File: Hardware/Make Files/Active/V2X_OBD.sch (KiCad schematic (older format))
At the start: 87 parts, among them J1 DB9, P4 DB-9 to OBD2, P5 NVM_RST, Q1 2N7000, Q10 2N3904, Q2 BSS84, Q3 BSS84, Q4 BSS84, Q5 3906, Q6 2N3904, Q7 2N7000, Q8 2N3904, Q9 2N3904, SW1 SPST, U10 MCP2551, U5 ESDAxxSC6, U6 ESDAxxSC6, U7 STN1110, U8 LM339, U9 LM317, X2 16MHz

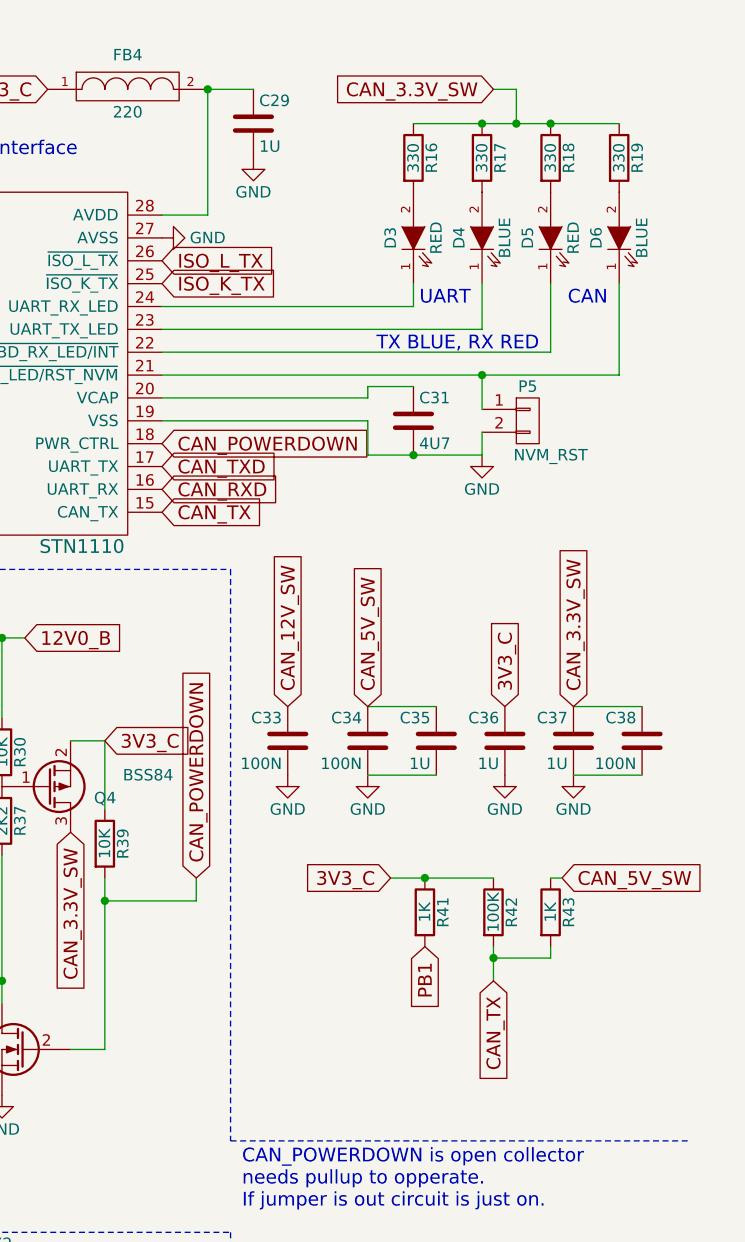
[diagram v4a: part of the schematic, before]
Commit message: Build pass of main V2X board
ready to verify
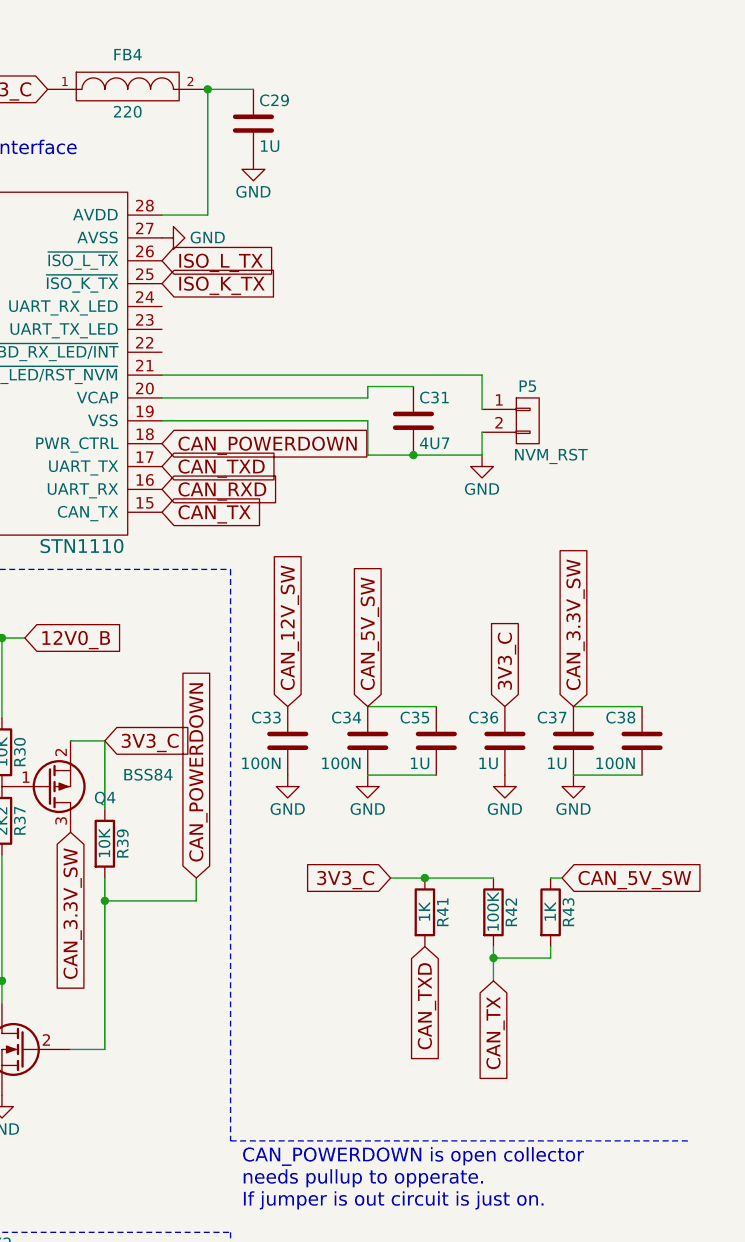
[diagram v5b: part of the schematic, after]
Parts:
- removed D3, D5: RED, LEDs:LED-0805, symbol LED
- removed D4, D6: BLUE, LEDs:LED-0805, symbol LED
- removed R16, R17, R18, R19: 330, Custom Parts:R_0603_sm, symbol R
- P5: footprint Connect:PINHEAD1-2 -> Custom Parts:R_0603_sm
- Q1, Q10, Q2, Q3, Q4, Q5, Q6, Q7, Q8, Q9: footprint Housings_SOT-23_SOT-143_TSOT-6:SOT-23 -> Custom Parts:SOT-23-123
- SW1: footprint Custom Parts:SW_SPST_A6TN_TH -> Custom Parts:SW_SPST_FSMSM_SM
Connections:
- net PB1 is gone; now on net CAN_TXD: R41.2
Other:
- note removed: "CAN"
- note removed: "TX BLUE, RX RED"
- note removed: "UART"
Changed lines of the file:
@@
 ISO_K_TX
-$Comp
-L R R16
-U 1 1 55A9FC84
-P 9900 1100
-F 0 "R16" V 9980 1100 50  0000 C CNN
-F 1 "330" V 9900 1100 50  0000 C CNN
-F 2 "Custom Parts:R_0603_sm" V 9830 1100 30  0001 C CNN
-F 3 "http://www.vishay.com/doc?20035" H 9900 1100 30  0001 C CNN
-F 4 "71-CRCW0603-330-E3" H 9900 1100 60  0001 C CNN "Mouse PN"
-	1    9900 1100
-	1    0    0    -1
-$EndComp
-Text Notes 10450 1950 2    60   ~ 0
-TX BLUE, RX RED
 $Comp
 L CONN_01X02 P5
@@
 F 0 "P5" H 10400 2400 50  0000 C CNN
 F 1 "NVM_RST" H 10500 2100 50  0000 C CNN
-F 2 "Connect:PINHEAD1-2" H 10400 2250 60  0001 C CNN
+F 2 "Custom Parts:R_0603_sm" H 10400 2250 60  0001 C CNN
 F 3 "http://www.mouser.com/ds/2/276/0022285023_PCB_HEADERS-159058.pdf" H 10400 2250 60  0001 C CNN
 F 4 "538-22-28-5023" H 10400 2250 60  0001 C CNN "Mouse PN"
@@
 	1    0    0    -1
 $EndComp
-Text Notes 10150 1750 2    60   ~ 0
-UART
-Text Notes 10750 1750 2    60   ~ 0
-CAN
 Text GLabel 8800 2650 2    60   Input ~ 0
 CAN_TX
@@
 F 0 "Q6" H 5000 4300 50  0000 R CNN
 F 1 "2N3904" H 5100 4400 50  0000 R CNN
-F 2 "Housings_SOT-23_SOT-143_TSOT-6:SOT-23" H 4900 4450 29  0001 C CNN
+F 2 "Custom Parts:SOT-23-123" H 4900 4450 29  0001 C CNN
 F 3 "http://www.mouser.com/ds/2/395/MMBT3904_D14-536637.pdf" H 4700 4350 60  0001 C CNN
 F 4 "821-MMBT3904" H 4700 4350 60  0001 C CNN "Mouse PN"
@@
 F 0 "Q5" H 5700 4100 50  0000 R CNN
 F 1 "3906" H 5800 4000 50  0000 R CNN
-F 2 "Housings_SOT-23_SOT-143_TSOT-6:SOT-23" H 5600 4150 29  0001 C CNN
+F 2 "Custom Parts:SOT-23-123" H 5600 4150 29  0001 C CNN
 F 3 "http://www.mouser.com/ds/2/115/ds30059-15980.pdf" H 5400 4050 60  0001 C CNN
 F 4 "621-MMBT3906-F" H 5400 4050 60  0001 C CNN "Mouse PN"
@@
 F 0 "Q4" H 8600 3900 50  0000 R CNN
 F 1 "BSS84" H 8850 3800 50  0000 R CNN
-F 2 "Housings_SOT-23_SOT-143_TSOT-6:SOT-23" H 8500 3950 29  0001 C CNN
+F 2 "Custom Parts:SOT-23-123" H 8500 3950 29  0001 C CNN
 F 3 "http://www.mouser.com/ds/2/149/BSS84-39462.pdf" H 8300 3850 60  0001 C CNN
 F 4 "512-BSS84" H 8300 3850 60  0001 C CNN "Mouse PN"
@@
 	1    0    0    -1
 $EndComp
-Text GLabel 10250 800  0    60   Input ~ 0
-CAN_3.3V_SW
 Text GLabel 5150 1100 0    60   Input ~ 0
 BAT_SAMPLE
@@
 	9000 1350 8800 1350
 Wire Wire Line
-	10200 1450 10200 1450
-Wire Wire Line
-	10800 1450 10800 1450
-Wire Wire Line
-	9900 1450 9900 1450
-Wire Wire Line
-	10500 1450 10500 1450
-Wire Wire Line
-	9900 1750 9900 1650
-Wire Wire Line
-	8800 1850 10200 1850
-Wire Wire Line
-	10200 1850 10200 1650
-Wire Wire Line
-	10500 1950 10500 1650
-Wire Wire Line
 	10200 2400 10200 2300
 Wire Wire Line
@@
 Connection ~ 9950 4250
 Wire Wire Line
-	8800 1750 9900 1750
-Connection ~ 10500 950
-Connection ~ 10200 950
-Wire Wire Line
-	10500 1950 8800 1950
-Wire Wire Line
-	8800 2050 10800 2050
-Wire Wire Line
-	10800 2050 10800 1650
-Wire Wire Line
 	10200 2200 10200 2050
-Connection ~ 10200 2050
 Wire Wire Line
 	9000 800  9000 1350
@@
 Wire Wire Line
 	4850 1600 5500 1600
-Wire Wire Line
-	9900 950  10800 950
-Wire Wire Line
-	10250 800  10350 800
-Wire Wire Line
-	10350 800  10350 950
-Connection ~ 10350 950
 Wire Notes Line
 	6200 2900 9100 2900
@@
 Text GLabel 8800 2550 2    60   Input ~ 0
 CAN_RXD
-Text GLabel 9950 4550 3    60   Input ~ 0
-PB1
 Text GLabel 9500 6100 0    60   Input ~ 0
 CAN_H
@@
 F 0 "SW1" H 10000 6200 50  0000 C CNN
 F 1 "SPST" H 10000 6000 50  0000 C CNN
-F 2 "Custom Parts:SW_SPST_A6TN_TH" H 10000 6100 60  0001 C CNN
+F 2 "Custom Parts:SW_SPST_FSMSM_SM" H 10000 6100 60  0001 C CNN
 F 3 "http://www.mouser.com/ds/2/307/en-a6tn-17713.pdf" H 10000 6100 60  0001 C CNN
 F 4 "653-A6TN-1104" H 10000 6100 60  0001 C CNN "Mouse PN"
@@
 $EndComp
 $Comp
-L LED D5
-U 1 1 56049D6C
-P 10500 1450
-F 0 "D5" H 10500 1550 50  0000 C CNN
-F 1 "RED" H 10500 1350 50  0000 C CNN
-F 2 "LEDs:LED-0805" H 10500 1450 60  0001 C CNN
-F 3 "http://www.mouser.com/ds/2/311/LS%20R976%20-%20CHIPLED%200805-318756.pdf" H 10500 1450 60  0001 C CNN
-F 4 "720-LSR976-NR-1" H 10500 1450 60  0001 C CNN "Mouse PN"
-	1    10500 1450
-	0    -1   -1   0
-$EndComp
-$Comp
-L LED D6
-U 1 1 56049D74
-P 10800 1450
-F 0 "D6" H 10800 1550 50  0000 C CNN
-F 1 "BLUE" H 10800 1350 50  0000 C CNN
-F 2 "LEDs:LED-0805" H 10800 1450 60  0001 C CNN
-F 3 "http://www.mouser.com/ds/2/445/150080BS75000-368924.pdf" H 10800 1450 60  0001 C CNN
-F 4 "710-150080BS75000" H 10800 1450 60  0001 C CNN "Mouse PN"
-	1    10800 1450
-	0    -1   -1   0
-$EndComp
-$Comp
-L LED D3
-U 1 1 56049F71
-P 9900 1450
-F 0 "D3" H 9900 1550 50  0000 C CNN
-F 1 "RED" H 9900 1350 50  0000 C CNN
-F 2 "LEDs:LED-0805" H 9900 1450 60  0001 C CNN
-F 3 "http://www.mouser.com/ds/2/311/LS%20R976%20-%20CHIPLED%200805-318756.pdf" H 9900 1450 60  0001 C CNN
-F 4 "720-LSR976-NR-1" H 9900 1450 60  0001 C CNN "Mouse PN"
-	1    9900 1450
-	0    -1   -1   0
-$EndComp
-$Comp
-L LED D4
-U 1 1 5604A2CE
-P 10200 1450
-F 0 "D4" H 10200 1550 50  0000 C CNN
-F 1 "BLUE" H 10200 1350 50  0000 C CNN
-F 2 "LEDs:LED-0805" H 10200 1450 60  0001 C CNN
-F 3 "http://www.mouser.com/ds/2/445/150080BS75000-368924.pdf" H 10200 1450 60  0001 C CNN
-F 4 "710-150080BS75000" H 10200 1450 60  0001 C CNN "Mouse PN"
-	1    10200 1450
-	0    -1   -1   0
-$EndComp
-$Comp
-L R R17
-U 1 1 5604C238
-P 10200 1100
-F 0 "R17" V 10280 1100 50  0000 C CNN
-F 1 "330" V 10200 1100 50  0000 C CNN
-F 2 "Custom Parts:R_0603_sm" V 10130 1100 30  0001 C CNN
-F 3 "http://www.vishay.com/doc?20035" H 10200 1100 30  0001 C CNN
-F 4 "71-CRCW0603-330-E3" H 10200 1100 60  0001 C CNN "Mouse PN"
-	1    10200 1100
-	1    0    0    -1
-$EndComp
-$Comp
-L R R18
-U 1 1 5604C35F
-P 10500 1100
-F 0 "R18" V 10580 1100 50  0000 C CNN
-F 1 "330" V 10500 1100 50  0000 C CNN
-F 2 "Custom Parts:R_0603_sm" V 10430 1100 30  0001 C CNN
-F 3 "http://www.vishay.com/doc?20035" H 10500 1100 30  0001 C CNN
-F 4 "71-CRCW0603-330-E3" H 10500 1100 60  0001 C CNN "Mouse PN"
-	1    10500 1100
-	1    0    0    -1
-$EndComp
-$Comp
-L R R19
-U 1 1 5604C48B
-P 10800 1100
-F 0 "R19" V 10880 1100 50  0000 C CNN
-F 1 "330" V 10800 1100 50  0000 C CNN
-F 2 "Custom Parts:R_0603_sm" V 10730 1100 30  0001 C CNN
-F 3 "http://www.vishay.com/doc?20035" H 10800 1100 30  0001 C CNN
-F 4 "71-CRCW0603-330-E3" H 10800 1100 60  0001 C CNN "Mouse PN"
-	1    10800 1100
-	1    0    0    -1
-$EndComp
-$Comp
 L C C35
 U 1 1 5604DEF3
@@
 F 0 "Q3" H 7750 3900 50  0000 R CNN
 F 1 "BSS84" H 8000 3800 50  0000 R CNN
-F 2 "Housings_SOT-23_SOT-143_TSOT-6:SOT-23" H 7650 3950 29  0001 C CNN
+F 2 "Custom Parts:SOT-23-123" H 7650 3950 29  0001 C CNN
 F 3 "http://www.mouser.com/ds/2/149/BSS84-39462.pdf" H 7450 3850 60  0001 C CNN
 F 4 "512-BSS84" H 7450 3850 60  0001 C CNN "Mouse PN"
@@
 F 0 "Q2" H 6900 3900 50  0000 R CNN
 F 1 "BSS84" H 7150 3800 50  0000 R CNN
-F 2 "Housings_SOT-23_SOT-143_TSOT-6:SOT-23" H 6800 3950 29  0001 C CNN
+F 2 "Custom Parts:SOT-23-123" H 6800 3950 29  0001 C CNN
 F 3 "http://www.mouser.com/ds/2/149/BSS84-39462.pdf" H 6600 3850 60  0001 C CNN
 F 4 "512-BSS84" H 6600 3850 60  0001 C CNN "Mouse PN"
@@
 F 0 "Q7" H 8500 5050 50  0000 R CNN
 F 1 "2N7000" H 8700 4950 50  0000 R CNN
-F 2 "Housings_SOT-23_SOT-143_TSOT-6:SOT-23" H 8400 5100 29  0001 C CNN
+F 2 "Custom Parts:SOT-23-123" H 8400 5100 29  0001 C CNN
 F 3 "http://www.mouser.com/ds/2/149/2N7002K-102052.pdf" H 8200 5000 60  0001 C CNN
 F 4 "512-2N7002K" H 8200 5000 60  0001 C CNN "Mouse PN"
@@
 F 0 "Q8" H 2650 5200 50  0000 R CNN
 F 1 "2N3904" H 2750 5300 50  0000 R CNN
-F 2 "Housings_SOT-23_SOT-143_TSOT-6:SOT-23" H 2550 5350 29  0001 C CNN
+F 2 "Custom Parts:SOT-23-123" H 2550 5350 29  0001 C CNN
 F 3 "http://www.mouser.com/ds/2/395/MMBT3904_D14-536637.pdf" H 2350 5250 60  0001 C CNN
 F 4 "821-MMBT3904" H 2350 5250 60  0001 C CNN "Mouse PN"
@@
 F 0 "Q10" V 1550 6950 50  0000 R CNN
 F 1 "2N3904" V 1650 7100 50  0000 R CNN
-F 2 "Housings_SOT-23_SOT-143_TSOT-6:SOT-23" H 1600 7200 29  0001 C CNN
+F 2 "Custom Parts:SOT-23-123" H 1600 7200 29  0001 C CNN
 F 3 "http://www.mouser.com/ds/2/395/MMBT3904_D14-536637.pdf" H 1400 7100 60  0001 C CNN
 F 4 "821-MMBT3904" H 1400 7100 60  0001 C CNN "Mouse PN"
@@
 F 0 "Q9" V 1450 6300 50  0000 R CNN
 F 1 "2N3904" V 1350 6400 50  0000 R CNN
-F 2 "Housings_SOT-23_SOT-143_TSOT-6:SOT-23" H 1600 6600 29  0001 C CNN
+F 2 "Custom Parts:SOT-23-123" H 1600 6600 29  0001 C CNN
 F 3 "http://www.mouser.com/ds/2/395/MMBT3904_D14-536637.pdf" H 1400 6500 60  0001 C CNN
 F 4 "821-MMBT3904" H 1400 6500 60  0001 C CNN "Mouse PN"
@@
 F 0 "Q1" H 3950 3900 50  0000 R CNN
 F 1 "2N7000" H 4050 3600 50  0000 R CNN
-F 2 "Housings_SOT-23_SOT-143_TSOT-6:SOT-23" H 4400 3850 29  0001 C CNN
+F 2 "Custom Parts:SOT-23-123" H 4400 3850 29  0001 C CNN
 F 3 "http://www.mouser.com/ds/2/149/2N7002K-102052.pdf" H 4200 3750 60  0001 C CNN
 F 4 "512-2N7002K" H 4200 3750 60  0001 C CNN "Mouse PN"
@@
 Text GLabel 8300 6050 2    60   Input ~ 0
 CAN_CLKN
+Wire Wire Line
+	10200 2050 8800 2050
+Text GLabel 9950 4550 3    60   Input ~ 0
+CAN_TXD
 $EndSCHEMATC

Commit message: V1.2 pass complete and ready to order
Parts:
- P4: Mouse PN NA -> (none)
- U7: Mouse PN SOIC-28 -> (none)
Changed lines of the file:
@@
 F 2 "Housings_SOIC:SOIC-28_7.5x17.9mm_Pitch1.27mm" H 7550 1750 60  0001 C CNN
 F 3 "https://www.scantool.net/dev-tools/stn11xx/stn1110.html?utm_source=obdsol&utm_medium=btn&utm_campaign=stn1110-order" H 7550 1750 60  0001 C CNN
-F 4 "SOIC-28" H 7550 1750 60  0001 C CNN "Mouse PN"
 	1    7550 1750
 	1    0    0    -1
@@
 F 2 "" H 750 1550 60  0001 C CNN
 F 3 "http://www.amazon.com/Adapter-Cable--Connecting-Diagnostic-Interface-Compliant/dp/B007UKTW8E/ref=sr_1_1?ie=UTF8&qid=1443117694&sr=8-1" H 750 1550 60  0001 C CNN
-F 4 "NA" H 750 1550 60  0001 C CNN "Mouse PN"
 	1    750  1550
 	1    0    0    -1
@@
 Text GLabel 9950 4550 3    60   Input ~ 0
 CAN_TXD
+Entry Bus Bus
+	6700 200  6800 300
 $EndSCHEMATC

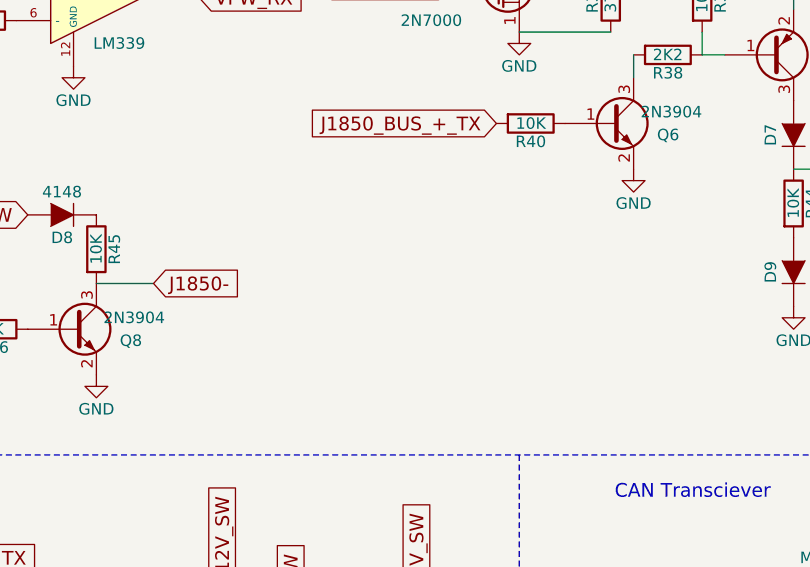
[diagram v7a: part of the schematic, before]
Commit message: Added USB-A to design
discovered the Rpi cannot be back fed over USB, had to add a power Port
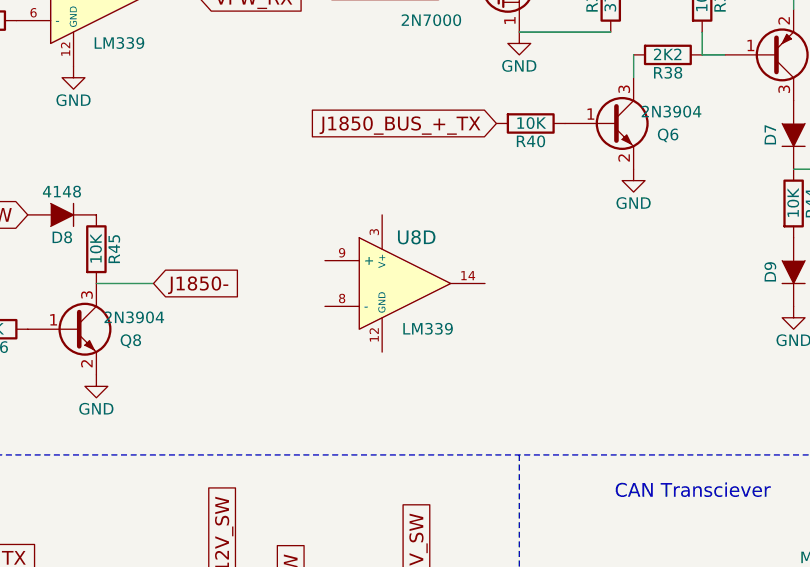
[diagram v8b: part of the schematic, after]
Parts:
- added unit 4 of U8
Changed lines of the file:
@@
 $Descr A4 11693 8268
 encoding utf-8
-Sheet 3 7
+Sheet 3 8
 Title "V2X - Open source RVI over SMS daughter card"
 Date "2015-07-17"
@@
 Entry Bus Bus
 	6700 200  6800 300
+$Comp
+L LM339 U8
+U 4 1 561EFD20
+P 3800 5050
+F 0 "U8" H 3850 5250 60  0000 C CNN
+F 1 "LM339" H 3900 4850 50  0000 C CNN
+F 2 "Housings_SOIC:SOIC-14_3.9x8.7mm_Pitch1.27mm" H 3800 5050 60  0001 C CNN
+F 3 "http://www.ti.com/lit/gpn/lm339a" H 3800 5050 60  0001 C CNN
+F 4 "LM339ADR" H 3800 5050 60  0001 C CNN "Mouse PN"
+	4    3800 5050
+	1    0    0    -1
+$EndComp
 $EndSCHEMATC
